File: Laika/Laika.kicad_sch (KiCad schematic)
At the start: 12 parts, among them J2 Micro_SD_Card, U1 LSM6DSL, U2 MS5611-01BA, U3 RASPBERRY_PI_ZERO_2_W

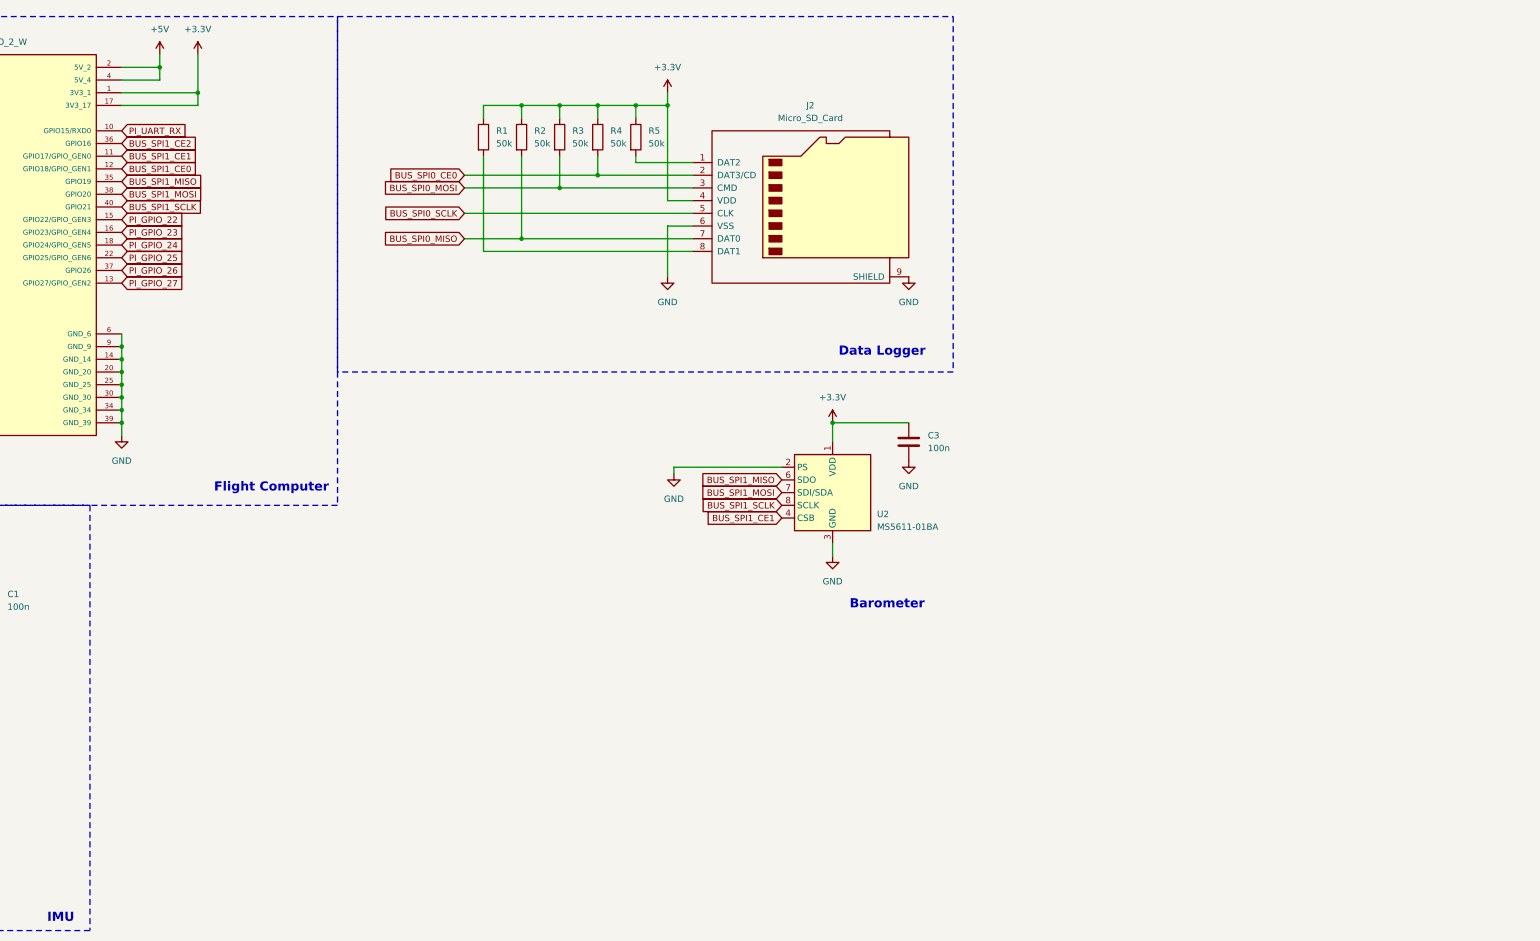
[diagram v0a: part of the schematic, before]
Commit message: Schematic for sensors
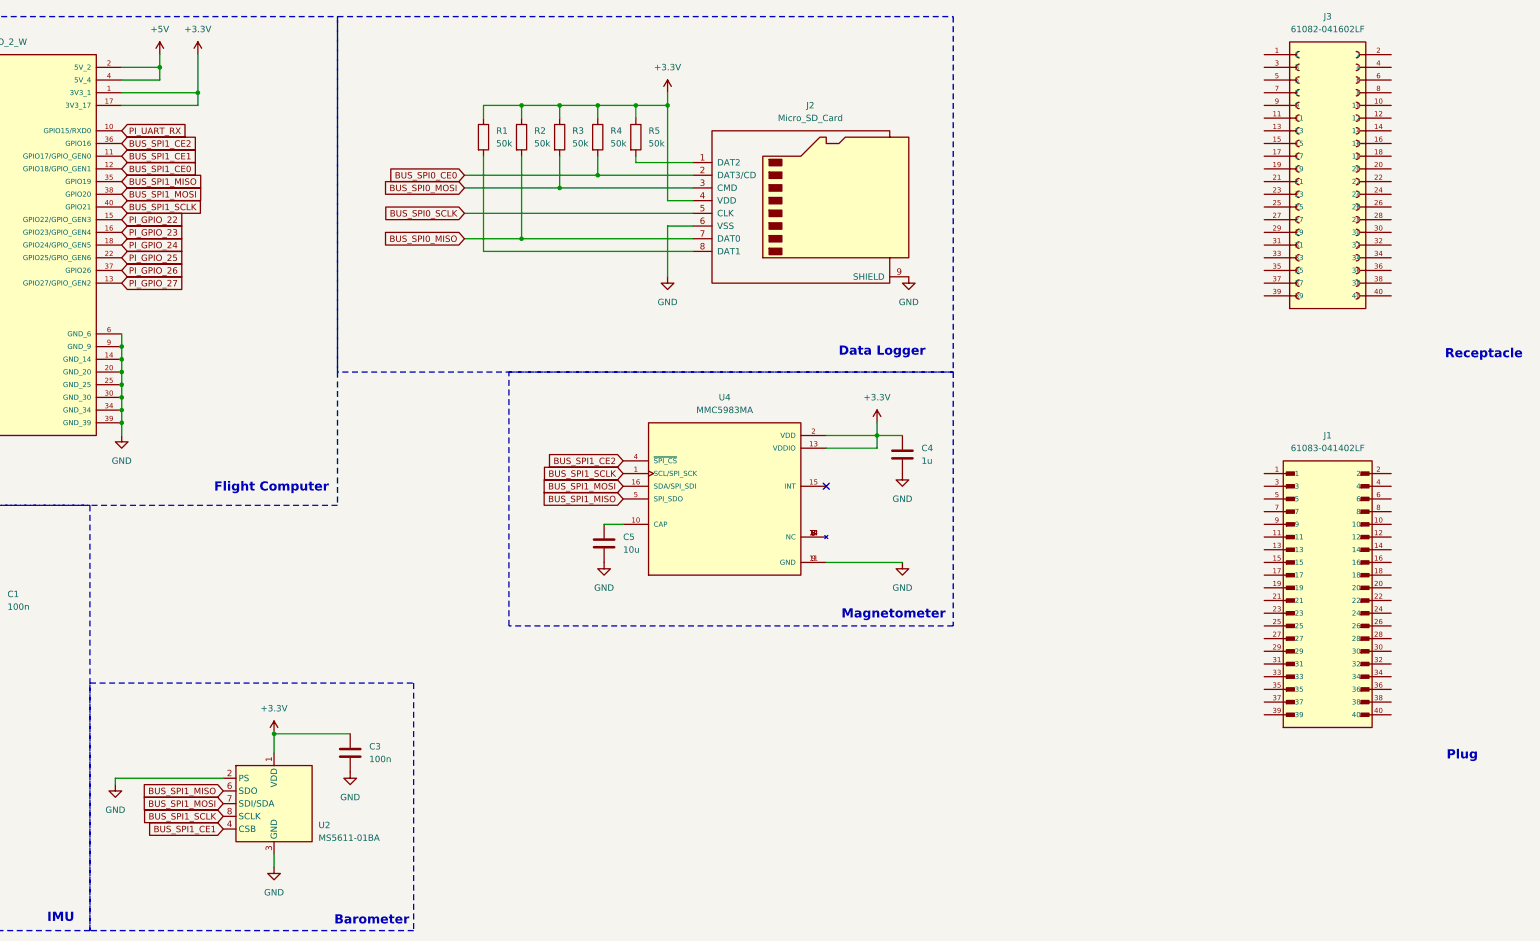
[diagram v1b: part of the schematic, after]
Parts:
- added C4: 1u, Capacitor_SMD:C_1206_3216Metric, symbol Device:C
- added C5: 10u, Capacitor_SMD:C_1206_3216Metric, symbol Device:C
- added J1: 61083-041402LF, 61083-041402LF:AMPHENOL_61083-041402LF, symbol 61083-041402LF:61083-041402LF
- added J3: 61082-041602LF, 61082-041602LF:AMPHENOL_61082-041602LF, symbol 61082-041602LF:61082-041602LF
- added U4: MMC5983MA, MMC5983MA:MMC5983_PQFN50, symbol MMC5983MA:MMC5983MA
- C1, C2, C3: footprint (none) -> Capacitor_SMD:C_1206_3216Metric
- R1, R2, R3, R4, R5: footprint (none) -> Resistor_SMD:R_1210_3225Metric
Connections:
- net +3.3V: now also C4.1, U4.13 (VDDIO), U4.2 (VDD)
- net BUS_SPI1_CE2: now also U4.4 (~{SPI_CS})
- net BUS_SPI1_MISO: now also U4.5 (SPI_SDO)
- net BUS_SPI1_MOSI: now also U4.16 (SDA/SPI_SDI)
- net BUS_SPI1_SCLK: now also U4.1 (SCL/SPI_SCK)
- net GND: now also C4.2, C5.2, U4.11 (GND), U4.9 (GND)
- new net: C5.1, U4.10 (CAP)
- new net: U4.12 (NC), U4.14 (NC), U4.3 (NC), U4.6 (NC), U4.7 (NC), U4.8 (NC)
- no-connect marks 2 -> 3
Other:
- note added: "Magnetometer"
- note added: "Plug"
- note added: "Receptacle"
- moved on the sheet: C3, U2

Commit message: RS485 hookup, new accelerometer, connectors, edgecuts
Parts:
- removed J1: 61083-041402LF, 61083-041402LF:AMPHENOL_61083-041402LF, symbol 61083-041402LF:61083-041402LF
- removed J3: 61082-041602LF, 61082-041602LF:AMPHENOL_61082-041602LF, symbol 61082-041602LF:61082-041602LF
- added C6: 100n, Capacitor_SMD:C_0603_1608Metric, symbol Device:C
- added C7: 10u, Capacitor_SMD:C_0603_1608Metric, symbol Device:C
- added D1, D2: CDSOT23-SM712, CDSOT23-SM712:SOT23-3, symbol CDSOT23-SM712:CDSOT23-SM712
- added J1: A-DF_09_A_KG-T4S, A-DF 09 AKG-T4S:ASSMANN_A-DF_09_A_KG-T4S, symbol A-DF_09_A_KG-T4S:A-DF_09_A_KG-T4S
- added J3: 0436500300, 0436500300:MOLEX_0436500300, symbol 0436500300:0436500300
- added R10, R11: R, Resistor_SMD:R_1206_3216Metric, symbol Device:R
- added R6, R7, R8, R9: 10, Resistor_SMD:R_1206_3216Metric, symbol Device:R
- added U5: H3LIS331DLTR, H3LIS331DLTR:QFN300X300X100-16N, symbol H3LIS331DLTR:H3LIS331DLTR
- added U6: THVD1451D, Package_SO:SOIC-8_3.9x4.9mm_P1.27mm, symbol Interface_UART:THVD1451D
- C1, C2, C3, C4, C5: footprint Capacitor_SMD:C_1206_3216Metric -> Capacitor_SMD:C_0603_1608Metric
- R1, R2, R3, R4, R5: footprint Resistor_SMD:R_1210_3225Metric -> Resistor_SMD:R_1206_3216Metric
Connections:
- net +3.3V: now also C6.1, C7.1, U5.1 (VDD_IO), U5.14 (VDD), U5.15 (VDD), U6.1 (VCC)
- net +5V: now also J3.1
- net BUS_SPI1_MISO: now also U5.7 (SDO/SA0)
- net BUS_SPI1_MOSI: now also U5.6 (SDA/SDI/SDO)
- net BUS_SPI1_SCLK: now also U5.4 (SCL/SPC)
- net GND: now also C6.2, C7.2, D1.3, D2.3, J1.5, J1.S1 (SHIELD), J1.S2 (SHIELD), J3.2, U5.10 (GND), U5.12 (GND), U5.13 (GND), U5.16 (GND), U5.5 (GND), U6.4 (GND)
- net PI_GPIO_27: now also U5.8 (CS)
- net PI_UART_RX: now also U6.2 (R)
- net PI_UART_TX: now also U6.3 (D)
- new net: R7.2, U6.5 (Y)
- new net: R8.2, U6.8 (A)
- new net: R6.2, U6.6 (Z)
- new net: R9.2, U6.7 (B)
- new net MODBUS_RX_N: D2.1, J1.8, R10.2, R9.1
- new net MODBUS_RX_P: D2.2, J1.2, R10.1, R8.1
- new net MODBUS_TX_N: D1.1, J1.9, R11.2, R7.1
- new net MODBUS_TX_P: D1.2, J1.3, R11.1, R6.1
- no-connect marks 3 -> 10
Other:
- note added: "Accelerometer 400-g"
- note added: "IMU 16-g"
- note added: "Power"
- note added: "RS485 Full Duplex Bus"
- note removed: "IMU"
- note removed: "Plug"
- note removed: "Receptacle"
- moved on the sheet: C1, C2, C3, C4, C5, J2, R1, R2, R3, R4, R5, U1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

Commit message: Version 0A
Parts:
- removed D1, D2: CDSOT23-SM712, CDSOT23-SM712:SOT23-3, symbol CDSOT23-SM712:CDSOT23-SM712
- removed J1: A-DF_09_A_KG-T4S, A-DF 09 AKG-T4S:ASSMANN_A-DF_09_A_KG-T4S, symbol A-DF_09_A_KG-T4S:A-DF_09_A_KG-T4S
- removed R10, R11: R, Resistor_SMD:R_1206_3216Metric, symbol Device:R
- removed R6, R7, R8, R9: 10, Resistor_SMD:R_1206_3216Metric, symbol Device:R
- removed U6: THVD1451D, Package_SO:SOIC-8_3.9x4.9mm_P1.27mm, symbol Interface_UART:THVD1451D
- added J1, J4: DF52-8S-0.8H_21_, Hirose D52:HIROSE_DF52-8S-0.8H_21_, symbol DF52-8S-0.8H_21_:DF52-8S-0.8H_21_
- added U6: PCA9685PW, Package_SO:TSSOP-28_4.4x9.7mm_P0.65mm, symbol Driver_LED:PCA9685PW
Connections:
- net +5V: now also U6.28 (VDD)
- net BUS_I2C1_SCL: now also U6.26 (SCL)
- net BUS_I2C1_SDA: now also U6.27 (SDA)
- net GND: now also J1.P1 (SHIELD), J1.P2 (SHIELD), J4.P1 (SHIELD), J4.P2 (SHIELD), U6.1 (A0), U6.14 (VSS), U6.2 (A1), U6.24 (A5), U6.3 (A2), U6.4 (A3), U6.5 (A4)
- net PI_GPIO_4: now also U6.23 (~{OE})
- new net PWM_0: J1.1, U6.6 (LED0)
- new net PWM_1: J1.2, U6.7 (LED1)
- new net PWM_10: J4.3, U6.17 (LED10)
- new net PWM_11: J4.4, U6.18 (LED11)
- new net PWM_12: J4.5, U6.19 (LED12)
- new net PWM_13: J4.6, U6.20 (LED13)
- new net PWM_14: J4.7, U6.21 (LED14)
- new net PWM_15: J4.8, U6.22 (LED15)
- new net PWM_2: J1.3, U6.8 (LED2)
- new net PWM_3: J1.4, U6.9 (LED3)
- new net PWM_4: J1.5, U6.10 (LED4)
- new net PWM_5: J1.6, U6.11 (LED5)
- new net PWM_6: J1.7, U6.12 (LED6)
- new net PWM_7: J1.8, U6.13 (LED7)
- new net PWM_8: J4.1, U6.15 (LED8)
- new net PWM_9: J4.2, U6.16 (LED9)
- no-connect marks 10 -> 7
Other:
- note added: "16 Channel PWM"
- note removed: "RS485 Full Duplex Bus"
